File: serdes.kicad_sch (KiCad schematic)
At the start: 11 parts

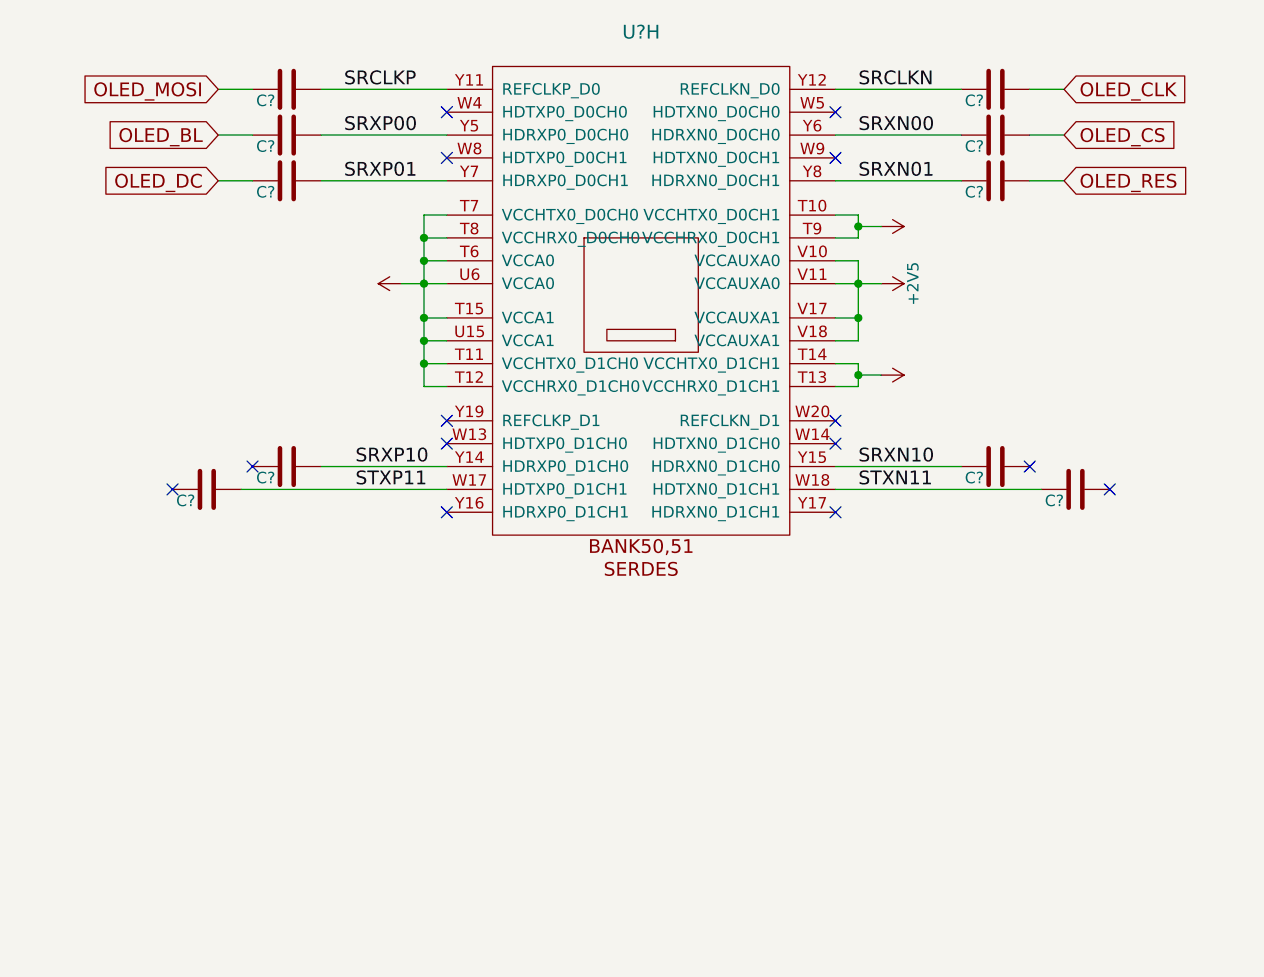
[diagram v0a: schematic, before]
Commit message: Adding USB-C
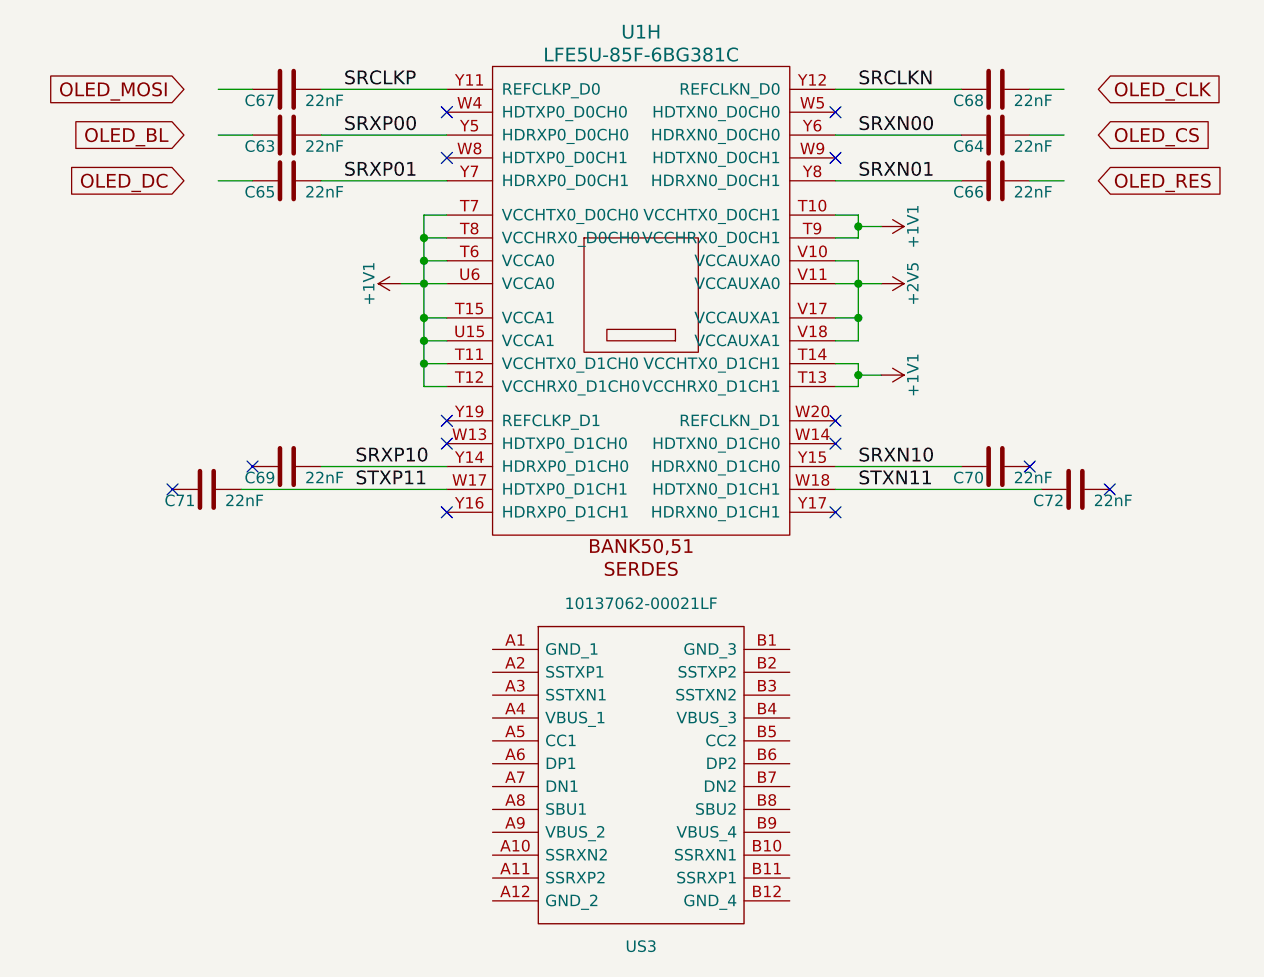
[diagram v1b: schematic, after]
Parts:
- added US3: 10137062-00021LF, USB-C:1013706200021LF, symbol 10137062-00021LF:10137062-00021LF
- C63, C64, C65, C66, C67, C68, C69, C70, C71, C72: renamed from C?; value (none) -> 22nF; footprint (none) -> Capacitor_SMD:C_0603_1608Metric
- U1: renamed from U?; value (none) -> LFE5U-85F-6BG381C; footprint (none) -> lfe5bg381:BGA-381_pitch0.8mm_dia0.4mm
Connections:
- net OLED_BL: no longer C63.1
- net OLED_CLK: no longer C68.2
- net OLED_CS: no longer C64.2
- net OLED_DC: no longer C65.1
- net OLED_MOSI: no longer C67.1
- net OLED_RES: no longer C66.2
